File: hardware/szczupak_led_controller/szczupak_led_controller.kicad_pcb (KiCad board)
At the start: 2 copper layers, 17 parts, among them IC1 STM32G0B1CBT6, J1 Conn_01x05

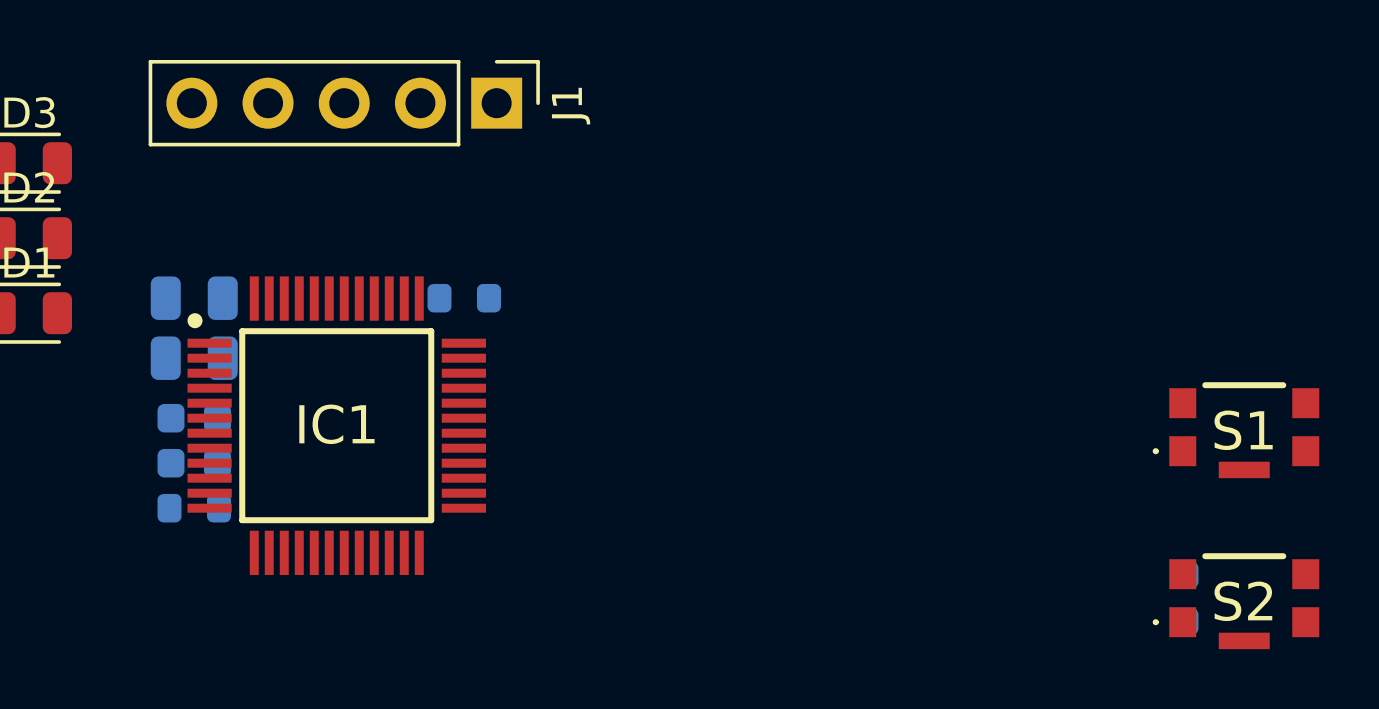
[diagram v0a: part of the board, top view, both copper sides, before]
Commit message: linked libraries and created pcb stack-up consistent with manufacturer data
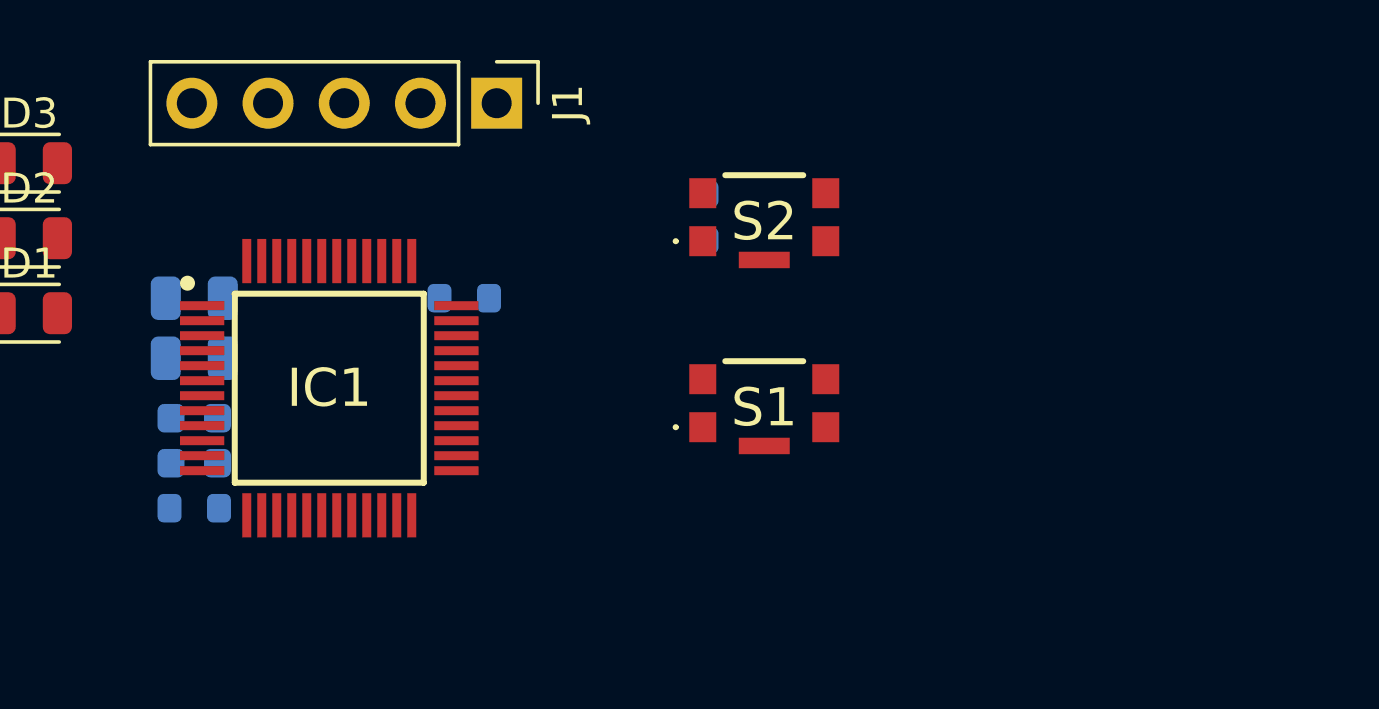
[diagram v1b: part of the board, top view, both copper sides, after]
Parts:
- IC1: footprint FOOTPRINTS:QFP50P900X900X160-48N -> szczupak_led_controller:QFP50P900X900X160-48N
- S1, S2: footprint FOOTPRINTS:KMR221GLFS -> szczupak_led_controller:KMR221GLFS
- moved C5 20.4 mm to (153.0, 87.3)
- moved S2 20.4 mm to (155.0, 87.3)
- moved S1 16.0 mm to (155.0, 93.5)
- moved IC1 1.27 mm to (140.5, 93.0)
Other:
- copper layers 2 -> 4

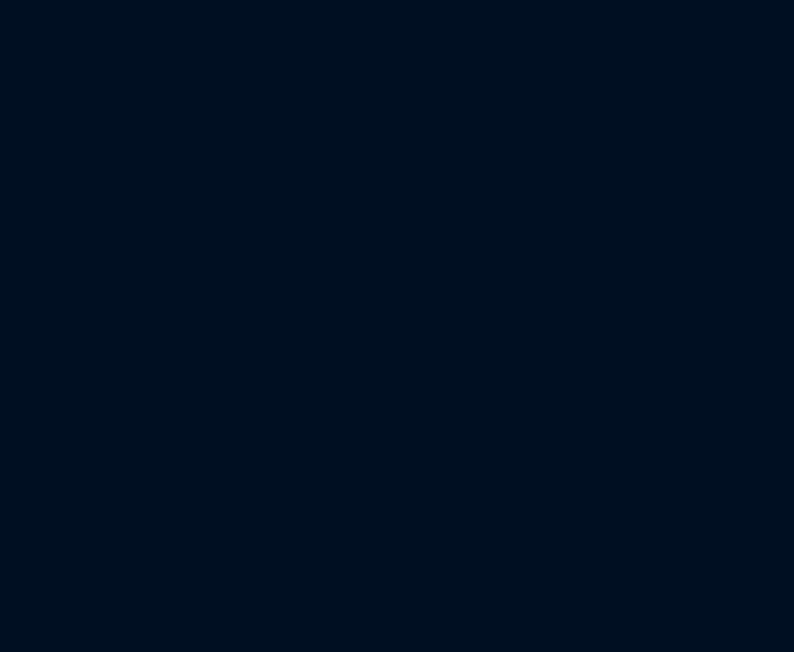
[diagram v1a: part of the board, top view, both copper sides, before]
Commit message: #3 Added some libraries for basic components in interfaces schematic
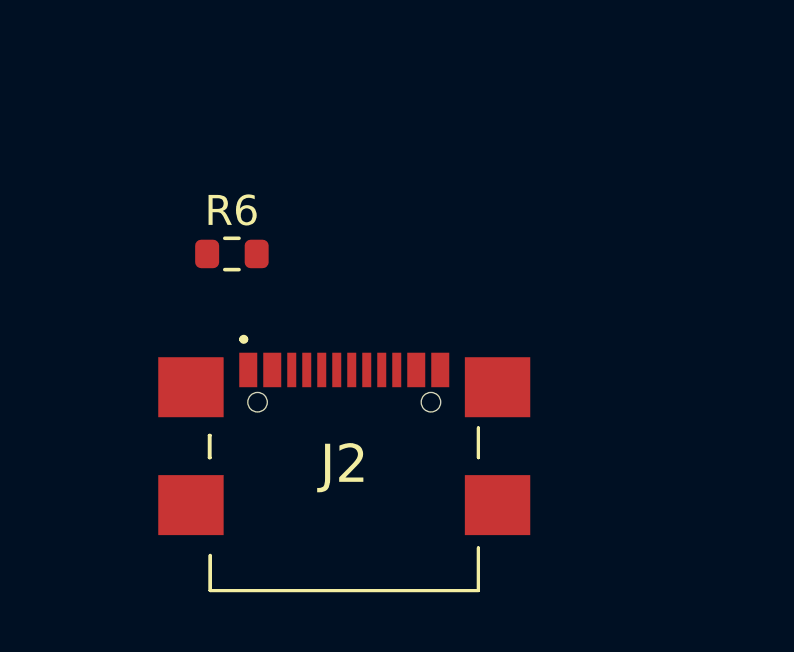
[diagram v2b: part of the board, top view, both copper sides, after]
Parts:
- added J2: USB4110-GF-A, szczupak_led_controller:USB4110GFA, F.Cu at (134.8, 116.8)
- added R6: 5k1, Resistor_SMD:R_0603_1608Metric, F.Cu at (131.0, 109.3)

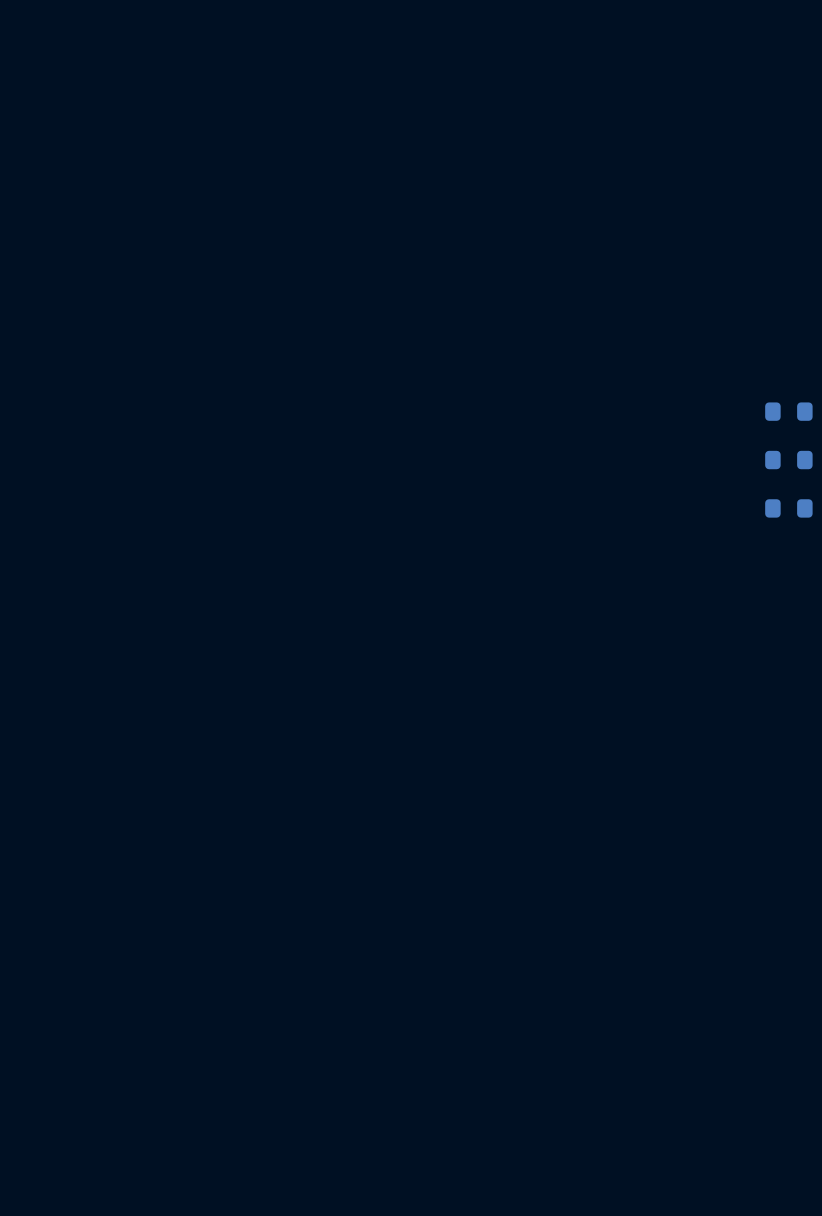
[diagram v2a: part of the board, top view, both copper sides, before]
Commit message: #5 #3 Added first version of power_input schematic with some required libraries
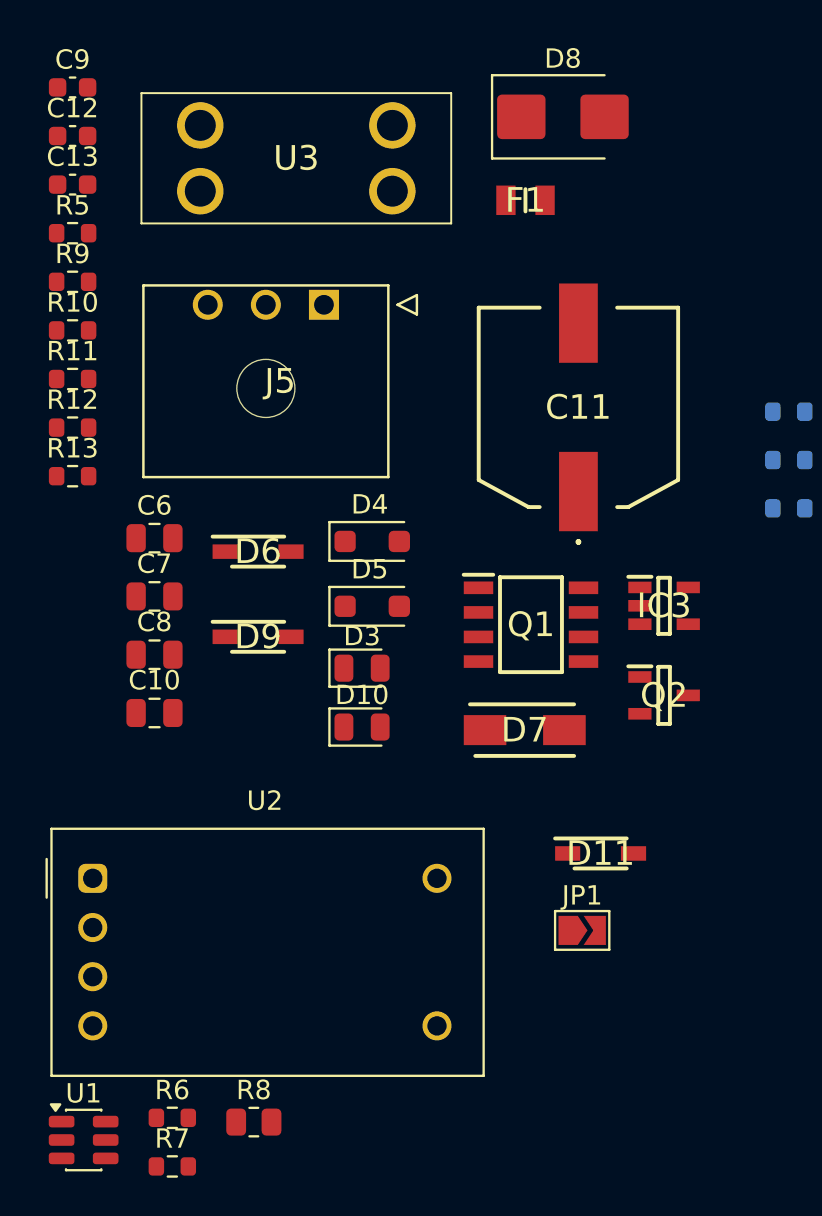
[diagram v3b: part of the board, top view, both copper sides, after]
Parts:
- added C10: 10uF, Capacitor_SMD:C_0805_2012Metric, F.Cu at (93.7, 101.1)
- added C11: 470uF, szczupak_led_controller:EEEFK1V331P, F.Cu at (115.6, 85.3)
- added C12: 100nF, Capacitor_SMD:C_0603_1608Metric, F.Cu at (89.5, 71.3)
- added C13: 100nF, Capacitor_SMD:C_0603_1608Metric, F.Cu at (89.5, 73.8)
- added C6: 1uF, Capacitor_SMD:C_0805_2012Metric, F.Cu at (93.7, 92.0)
- added C7: 1uF, Capacitor_SMD:C_0805_2012Metric, F.Cu at (93.7, 95.0)
- added C8: 10uF, Capacitor_SMD:C_0805_2012Metric, F.Cu at (93.7, 98.1)
- added C9: 100nF, Capacitor_SMD:C_0603_1608Metric, F.Cu at (89.5, 68.8)
- added D10: 12V LED, LED_SMD:LED_0805_2012Metric, F.Cu at (104.5, 101.8)
- added D11: STPS140Z, szczupak_led_controller:SOD3816X145N, F.Cu at (116.8, 108.3)
- added D3: 3V3 LED, LED_SMD:LED_0805_2012Metric, F.Cu at (104.5, 98.8)
- added D4: D_Zener, Diode_SMD:D_SOD-123F, F.Cu at (105.0, 92.2)
- added D5: D_Zener, Diode_SMD:D_SOD-123F, F.Cu at (105.0, 95.6)
- added D6: STPS140Z, szczupak_led_controller:SOD3816X145N, F.Cu at (99.1, 92.7)
- added D7: SMAJ5.0A-E3_61, szczupak_led_controller:DIOM5127X229N, F.Cu at (112.9, 102.0)
- added D8: SMBJ18A, Diode_SMD:D_SMB, F.Cu at (114.8, 70.3)
- added D9: STPS140Z, szczupak_led_controller:SOD3816X145N, F.Cu at (99.1, 97.1)
- added F1: 0ZCK0050FF2E, szczupak_led_controller:FUSC2214X125N, F.Cu at (112.9, 74.6)
- added IC3: TLV75533PDBVR, szczupak_led_controller:SOT95P280X145-5N, F.Cu at (120.1, 95.5)
- added J5: 43650-0300, szczupak_led_controller:436500300, F.Cu at (102.5, 80.0)
- added JP1: Jumper_2_Open, Jumper:SolderJumper-2_P1.3mm_Open_TrianglePad1.0x1.5mm, F.Cu at (115.8, 112.3)
- added Q1: AO4407A, szczupak_led_controller:SOIC127P600X175-8N, F.Cu at (113.2, 96.5)
- added Q2: AO3401A, szczupak_led_controller:SOT95P280X125-3N, F.Cu at (120.1, 100.2)
- added R10: 100k, Resistor_SMD:R_0603_1608Metric, F.Cu at (89.5, 81.3)
- added R11: 10k, Resistor_SMD:R_0603_1608Metric, F.Cu at (89.5, 83.8)
- added R12: 100k, Resistor_SMD:R_0603_1608Metric, F.Cu at (89.5, 86.3)
- added R13: 10k, Resistor_SMD:R_0603_1608Metric, F.Cu at (89.5, 88.8)
- added R5: 1k, Resistor_SMD:R_0603_1608Metric, F.Cu at (89.5, 76.3)
- added R6: 5.1k, Resistor_SMD:R_0603_1608Metric, F.Cu at (94.7, 122.0)
- added R7: 5.1k, Resistor_SMD:R_0603_1608Metric, F.Cu at (94.7, 124.5)
- added R8: 120, Resistor_SMD:R_0805_2012Metric, F.Cu at (98.9, 122.2)
- added R9: 100k, Resistor_SMD:R_0603_1608Metric, F.Cu at (89.5, 78.8)
- added U1: USBLC6-2SC6, Package_TO_SOT_SMD:SOT-23-6, F.Cu at (90.1, 123.1)
- added U2: RCD-24, Converter_DCDC:Converter_DCDC_RECOM_RCD-24_THT, F.Cu at (90.5, 109.6)
- added U3: 3568, szczupak_led_controller:3568, F.Cu at (96.1, 74.1)
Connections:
- J1 pad 5: +3.3V -> Net-(J1-Pin_5)
- S1 pad 3: unconnected-(S1-COM_2-Pad3) -> /02_mcu/SWCLK_BOOT0

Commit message: #4 #6 Added power output and interfaces schematics
Designed initial placement for most important components on pcb
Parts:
- removed the D3 at (104.5, 98.8)
- removed the D3 at (130.5, 85.5)
- removed the R5 at (89.5, 76.3)
- removed the R5 at (126.5, 85.5)
- removed the R6 at (94.7, 122.0)
- removed the R6 at (131.0, 109.3)
- removed U2: RCD-24, Converter_DCDC:Converter_DCDC_RECOM_RCD-24_THT
- added C14: UCD1C220MCL6GS, szczupak_led_controller:CAPAE430X610N, F.Cu at (122.9, 125.2)
- added C15: 100nF, Capacitor_SMD:C_0603_1608Metric, F.Cu at (349.1, 67.3)
- added C16: 1uF, Capacitor_SMD:C_0805_2012Metric, F.Cu at (354.1, 85.1)
- added C17: 4.7nF DNP, Capacitor_SMD:C_0603_1608Metric, F.Cu at (91.5, 113.0)
- added C18: 47pF DNP, Capacitor_SMD:C_0603_1608Metric, F.Cu at (84.5, 95.5)
- added C19: 47pF DNP, Capacitor_SMD:C_0603_1608Metric, F.Cu at (84.5, 90.5)
- added C20: 100nF, Capacitor_SMD:C_0603_1608Metric, F.Cu at (78.2, 84.4)
- added C21: 10uF, Capacitor_SMD:C_0805_2012Metric, B.Cu at (153.8, 51.2)
- added C22: 100nF, Capacitor_SMD:C_0603_1608Metric, F.Cu at (49.0, 84.0)
- added C23: 47pF DNP, Capacitor_SMD:C_0603_1608Metric, F.Cu at (83.0, 112.5)
- added C24: 100nF, Capacitor_SMD:C_0603_1608Metric, B.Cu at (151.6, 51.2)
- added C25: 100nF, Capacitor_SMD:C_0603_1608Metric, F.Cu at (130.0, 52.7)
- added C26: 100nF, Capacitor_SMD:C_0603_1608Metric, F.Cu at (113.5, 66.5)
- added C27: 100nF, Capacitor_SMD:C_0603_1608Metric, F.Cu at (249.2, 70.0)
- added C28: 100nF, Capacitor_SMD:C_0603_1608Metric, F.Cu at (249.3, 58.9)
- added C29: 100nF, Capacitor_SMD:C_0603_1608Metric, B.Cu at (150.1, 71.2)
- added C30: 10uF, Capacitor_SMD:C_0805_2012Metric, B.Cu at (152.1, 71.2)
- added C31: 100nF, Capacitor_SMD:C_0603_1608Metric, F.Cu at (249.3, 64.0)
- added C32: 100nF, Capacitor_SMD:C_0603_1608Metric, F.Cu at (253.3, 48.9)
- added C33: 100nF, Capacitor_SMD:C_0603_1608Metric, B.Cu at (150.1, 89.9)
- added C34: 10uF, Capacitor_SMD:C_0805_2012Metric, B.Cu at (152.1, 89.9)
- added C35: 47pF DNP, Capacitor_SMD:C_0603_1608Metric, F.Cu at (83.0, 117.5)
- added D12: PESD1CAN,215, szczupak_led_controller:SOT95P230X110-3N, F.Cu at (81.5, 93.0)
- added D13: PESD1CAN,215, szczupak_led_controller:SOT95P230X110-3N, F.Cu at (83.2, 115.0)
- added D3: LED 3V3, LED_SMD:LED_0805_2012Metric, F.Cu at (350.4, 24.9)
- added F2: 0ZCF0200FF2C, szczupak_led_controller:FUSC7451X90N, F.Cu at (120.4, 91.0)
- added F3: 0ZCF0200FF2C, szczupak_led_controller:FUSC7451X90N, F.Cu at (120.4, 98.5)
- added F4: 0ZCF0200FF2C, szczupak_led_controller:FUSC7451X90N, F.Cu at (120.5, 105.5)
- added F5: SM050-16, Fuse:Fuse_1210_3225Metric, F.Cu at (84.5, 64.9)
- added FL1: INA180A3IDBVR, szczupak_led_controller:SOT95P280X145-5N, F.Cu at (133.0, 53.2)
- added FL2: INA180A3IDBVR, szczupak_led_controller:SOT95P280X145-5N, F.Cu at (133.0, 74.2)
- added FL3: INA180A3IDBVR, szczupak_led_controller:SOT95P280X145-5N, F.Cu at (133.0, 91.2)
- added IC2: SN65HVD230DR, szczupak_led_controller:SOT127P600X175-8N, F.Cu at (89.5, 92.5)
- added J10: XT60PW-M, szczupak_led_controller:XT60PWM_shorter, F.Cu at (173.3, 88.4)
- added J3: CAN_CONN, szczupak_led_controller:XY2500V-D(5.08)-4PIN, F.Cu at (64.5, 121.5)
- added J4: 43650-0200, szczupak_led_controller:43650-02_00,01,02_, F.Cu at (133.9, 122.9)
- added J6: CAN_CONN, szczupak_led_controller:XY2500V-D(5.08)-4PIN, F.Cu at (64.5, 98.5)
- added J7: Conn_EXT, Connector_PinHeader_2.54mm:PinHeader_1x08_P2.54mm_Vertical, F.Cu at (344.8, 68.3)
- added J8: XT60PW-M, szczupak_led_controller:XT60PWM_shorter, F.Cu at (173.3, 49.8)
- added J9: XT60PW-M, szczupak_led_controller:XT60PWM_shorter, F.Cu at (173.3, 69.1)
- added JP2: SHIELD JMP, Jumper:SolderJumper-2_P1.3mm_Open_TrianglePad1.0x1.5mm, B.Cu at (80.3, 106.4)
- added JP3: SHIELD JMP, Jumper:SolderJumper-2_P1.3mm_Open_TrianglePad1.0x1.5mm, B.Cu at (80.5, 129.4)
- added PS1: RCD-24-1.00, szczupak_led_controller:RCD24030, F.Cu at (148.6, 49.6)
- added PS2: RCD-24-1.00, szczupak_led_controller:RCD24030, F.Cu at (147.2, 69.7)
- added PS3: RCD-24-1.00, szczupak_led_controller:RCD24030, F.Cu at (147.2, 87.9)
- added Q3: 2N7002, szczupak_led_controller:TRANS_2N7002, F.Cu at (120.5, 48.0)
- added Q4: 2N7002, szczupak_led_controller:TRANS_2N7002, F.Cu at (140.7, 80.7)
- added Q5: 2N7002, szczupak_led_controller:TRANS_2N7002, F.Cu at (138.6, 100.7)
- added R14: 10k, Resistor_SMD:R_0603_1608Metric, F.Cu at (353.1, 67.3)
- added R15: 33, Resistor_SMD:R_0603_1608Metric, F.Cu at (95.5, 90.5)
- added R16: 33, Resistor_SMD:R_0603_1608Metric, F.Cu at (95.5, 94.5)
- added R17: 60.4 DNP, Resistor_SMD:R_0805_2012Metric, F.Cu at (89.5, 116.5)
- added R18: 60.4 DNP, Resistor_SMD:R_0805_2012Metric, F.Cu at (89.5, 113.0)
- added R19: 0 DNP, Resistor_SMD:R_0603_1608Metric, B.Cu at (87.5, 88.5)
- added R20: 5.1k, Resistor_SMD:R_0603_1608Metric, F.Cu at (75.7, 63.9)
- added R21: 22, Resistor_SMD:R_0603_1608Metric, F.Cu at (92.8, 75.0)
- added R22: 22, Resistor_SMD:R_0603_1608Metric, F.Cu at (92.8, 73.0)
- added R23: 100k, Resistor_SMD:R_0603_1608Metric, F.Cu at (50.5, 80.7)
- added R24: 100k, Resistor_SMD:R_0603_1608Metric, F.Cu at (50.5, 84.0)
- added R25: 5.1k, Resistor_SMD:R_0603_1608Metric, F.Cu at (357.1, 72.3)
- added R26: 5.1k, Resistor_SMD:R_0603_1608Metric, F.Cu at (357.1, 74.8)
- added R27: 10k, Resistor_SMD:R_0603_1608Metric, F.Cu at (131.3, 34.5)
- added R28: 220, Resistor_SMD:R_0603_1608Metric, F.Cu at (116.5, 51.0)
- added R29: 100k, Resistor_SMD:R_0603_1608Metric, F.Cu at (117.5, 48.0)
- added R30: 1k, Resistor_SMD:R_0603_1608Metric, F.Cu at (253.3, 64.0)
- added R31: 10m SHUNT, Resistor_SMD:R_2512_6332Metric, F.Cu at (140.1, 73.7)
- added R32: 220, Resistor_SMD:R_0603_1608Metric, F.Cu at (257.3, 48.9)
- added R33: 10k, Resistor_SMD:R_0603_1608Metric, F.Cu at (257.3, 51.4)
- added R34: 100k, Resistor_SMD:R_0603_1608Metric, F.Cu at (257.3, 53.9)
- added R35: 1k, Resistor_SMD:R_0603_1608Metric, F.Cu at (257.3, 56.4)
- added R36: 10m SHUNT, Resistor_SMD:R_2512_6332Metric, F.Cu at (140.1, 91.2)
- added R37: 220, Resistor_SMD:R_0603_1608Metric, F.Cu at (257.3, 58.9)
- added R38: 10k, Resistor_SMD:R_0603_1608Metric, F.Cu at (257.3, 61.5)
- added R39: 100k, Resistor_SMD:R_0603_1608Metric, F.Cu at (257.3, 64.0)
- added R5: 1k, Resistor_SMD:R_0603_1608Metric, F.Cu at (321.6, 32.2)
- added R6: 10m SHUNT, Resistor_SMD:R_2512_6332Metric, F.Cu at (140.1, 53.7)
- C5, R3, R4: moved to F.Cu
- D10: value 12V LED -> LED 12V
- D11: moved to B.Cu
- F1: value 0ZCK0050FF2E -> SM050-16; footprint szczupak_led_controller:FUSC2214X125N -> Fuse:Fuse_1210_3225Metric
- JP1: value Jumper_2_Open -> SWD 3V3 POWER; moved to B.Cu
- R7: value 5.1k -> 1k
- R8: value 120 -> 5.1k; footprint Resistor_SMD:R_0805_2012Metric -> Resistor_SMD:R_0603_1608Metric
- moved C10 262.6 mm to (352.6, 57.0)
- moved C6 262.6 mm to (352.6, 48.0)
- moved C7 262.6 mm to (352.6, 51.0)
- moved C8 262.6 mm to (352.6, 54.0)
- moved D6 260.4 mm to (353.2, 35.5)
- moved D9 260.4 mm to (353.2, 39.9)
- moved D10 256.8 mm to (350.4, 28.0)
- moved IC3 245.4 mm to (355.3, 25.7)
- moved C9 236.2 mm to (321.6, 24.7)
- moved R11 236.2 mm to (321.6, 39.7)
- moved R12 236.2 mm to (321.6, 42.2)
- moved R13 236.2 mm to (321.6, 44.8)
- moved D2 118.7 mm to (27.2, 146.5)
- moved R4 118.7 mm to (23.2, 146.5), turned to 180 degrees
- moved R3 116.1 mm to (23.2, 143.5), turned to 180 degrees
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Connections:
- net /01_power_input/12V_PROT renamed /12V_LED
- net /01_power_input/R_gate renamed /01_power_input/Q1_GATE
- net Net-(D10-K) renamed /01_power_input/LED_12V_R
- net Net-(D11-A) renamed /02_mcu/3V3_PROG_D
- net Net-(D4-A) renamed /01_power_input/Q2_GATE
- net Net-(J1-Pin_5) renamed /02_mcu/3V3_PROG
- C7 pad 1: +3V3 -> +3.3V
- C8 pad 1: +3V3 -> +3.3V
- C9 pad 1: /01_power_input/ADC_12V -> /ADC_12V
- D6 pad 2: /01_power_input/USB_5V -> /01_power_input/USB_5V_FUSE
- IC1 pad 11: /02_mcu/ADC_LED1 -> /ADC_LED1
- IC1 pad 12: /02_mcu/ADC_LED2 -> /ADC_LED2
- IC1 pad 13: /02_mcu/ADC_LED3 -> /ADC_LED3
- IC1 pad 14: /02_mcu/ADC_12V -> /ADC_12V
- IC1 pad 15: /02_mcu/ADC_USB -> /ADC_USB
- IC1 pad 17: /02_mcu/PWM_LED1 -> /PWM_LED1
- IC1 pad 18: /02_mcu/PWM_LED2 -> /PWM_LED2
- IC1 pad 19: /02_mcu/PWM_LED3 -> /PWM_LED3
- IC1 pad 27: unconnected-(IC1-PB15-Pad27) -> /GPIO_EXT
- IC1 pad 28: unconnected-(IC1-PA8-Pad28) -> /PWM_EXT
- IC1 pad 29: /02_mcu/I2C1_SCL -> /I2C1_SCL
- IC1 pad 32: /02_mcu/I2C1_SDA -> /I2C1_SDA
- IC1 pad 33: /02_mcu/USB_DM -> /USB_D_MCU_N
- IC1 pad 34: /02_mcu/USB_DP -> /USB_D_MCU_P
- IC1 pad 45: /02_mcu/USART1_TX -> /USART1_TX
- IC1 pad 46: /02_mcu/USART1_RX -> /USART1_RX
- IC1 pad 47: /02_mcu/CAN_RX -> /CAN_RX
- IC1 pad 48: /02_mcu/CAN_TX -> /CAN_TX
- IC3 pad 5: +3V3 -> +3.3V
- J2 pad A1: unconnected-(J2-PadA1) -> GND
- J2 pad A12: unconnected-(J2-PadA12) -> GND
- J2 pad A4: VBUS -> /USB_5V
- J2 pad A5: Net-(J2-PadA5) -> /03_interfaces/CC1
- J2 pad A6: unconnected-(J2-PadA6) -> /03_interfaces/USB_D_P
- J2 pad A7: unconnected-(J2-PadA7) -> /03_interfaces/USB_D_N
- J2 pad A9: VBUS -> /USB_5V
- J2 pad B1: unconnected-(J2-PadB1) -> GND
- J2 pad B12: unconnected-(J2-PadB12) -> GND
- J2 pad B4: VBUS -> /USB_5V
- J2 pad B5: unconnected-(J2-PadB5) -> /03_interfaces/CC2
- J2 pad B6: unconnected-(J2-PadB6) -> /03_interfaces/USB_D_P
- J2 pad B7: unconnected-(J2-PadB7) -> /03_interfaces/USB_D_N
- J2 pad B9: VBUS -> /USB_5V
- R12 pad 2: /01_power_input/ADC_12V -> /ADC_12V
- R13 pad 1: /01_power_input/ADC_12V -> /ADC_12V
- R7 pad 1: Net-(J2-CC1) -> /ADC_LED1
- R7 pad 2: GND -> Net-(FL1-OUT)
- R8 pad 1: /03_interfaces/CANH -> /03_interfaces/CC1
- R8 pad 2: /03_interfaces/CANL -> GND
- U1 pad 1: Net-(J2-DN1) -> /03_interfaces/USB_D_N
- U1 pad 3: Net-(J2-DP1) -> /03_interfaces/USB_D_P
- U1 pad 4: /03_interfaces/USB_DP -> /03_interfaces/USB_D_ESD_P
- U1 pad 5: /03_interfaces/USB_5V -> /USB_5V
- U1 pad 6: /03_interfaces/USB_DM -> /03_interfaces/USB_D_ESD_N
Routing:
- net (no net): track 0.00 -> 1.50 mm
